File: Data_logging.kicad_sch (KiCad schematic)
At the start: 5 parts, among them J5 Micro_SD_Card_Det_Hirose_DM3AT, U9 47K

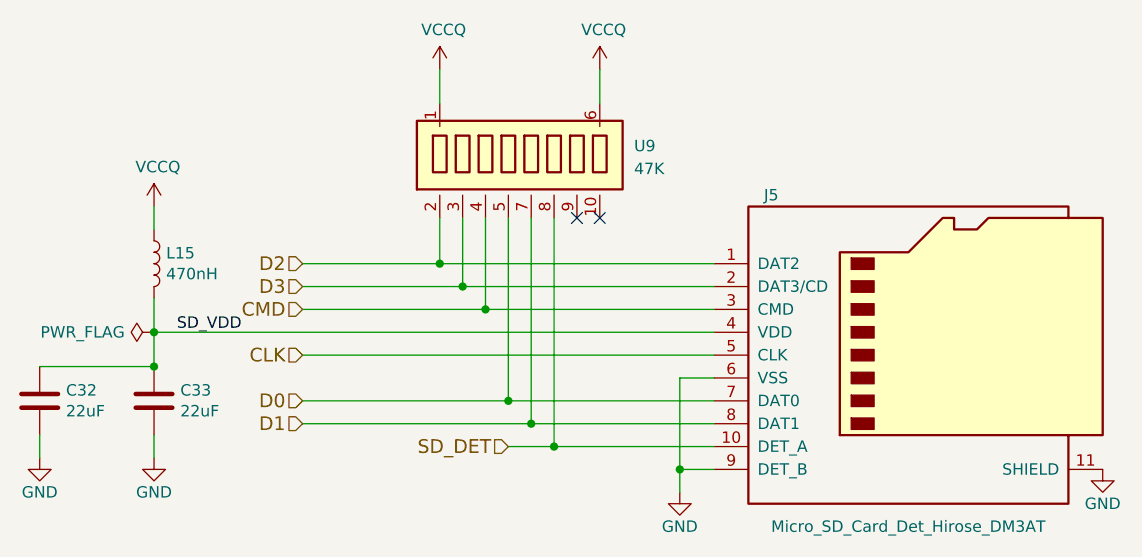
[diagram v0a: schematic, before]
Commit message: Reannotate schematic
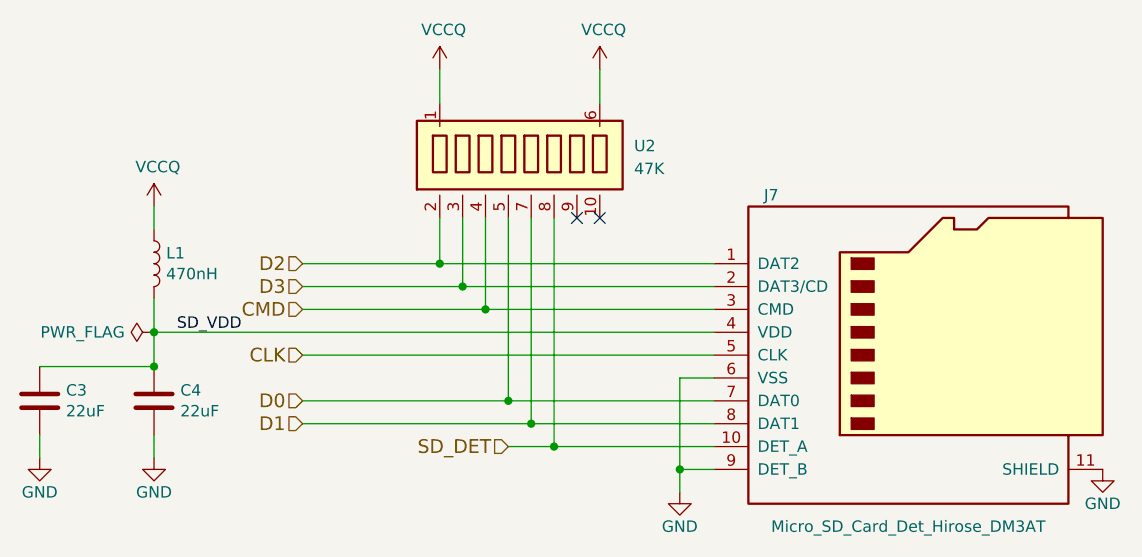
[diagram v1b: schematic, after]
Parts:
- renumbered C32 to C3, C33 to C4, J5 to J7, L15 to L1, U9 to U2
